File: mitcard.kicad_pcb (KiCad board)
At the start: 2 copper layers, 91 x 55 mm, 13 parts, among them J1 MJ-4PP-9, J2 MJ-4PP-9, SW1 SW_PUSH, SW2 SW_PUSH, SW3 SW_PUSH, SW4 SW_PUSH, U1 Teensy-LC

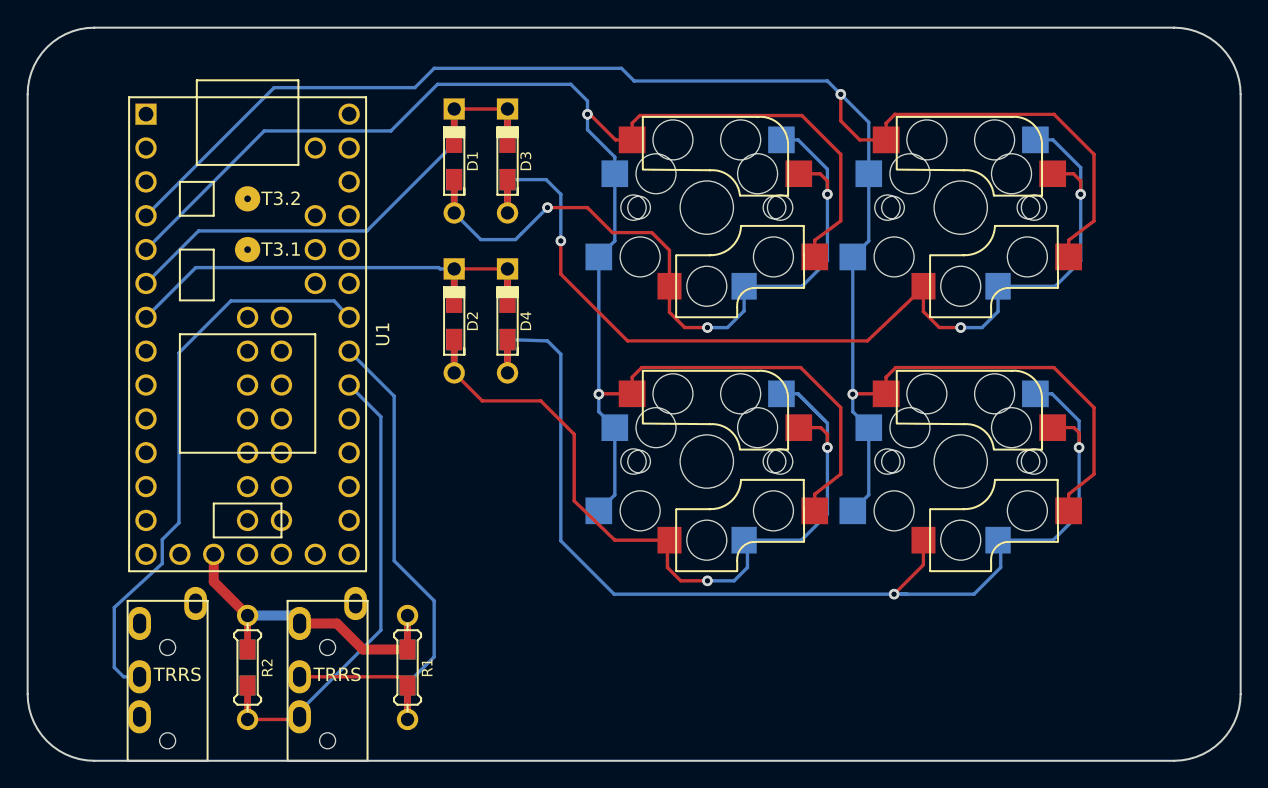
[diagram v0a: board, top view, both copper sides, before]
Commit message: タッチセンサー部を除いて仮配線完了？
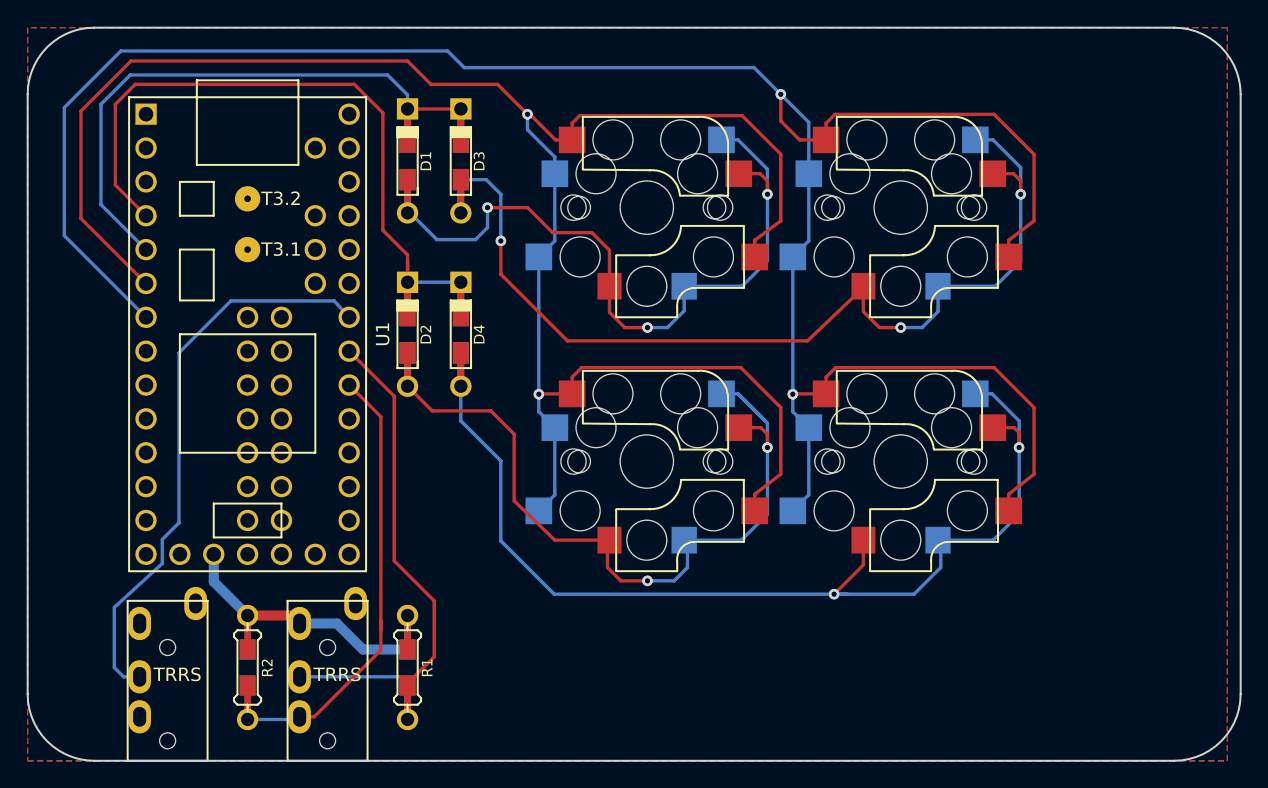
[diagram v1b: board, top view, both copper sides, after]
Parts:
- moved SW1 4.50 mm to (96.5, 63.5)
- moved SW2 4.50 mm to (96.5, 82.5)
- moved SW3 4.50 mm to (115.5, 63.5)
- moved SW4 4.50 mm to (115.5, 82.5)
- moved D2 3.64 mm to (78.5, 73.0)
- moved D4 3.64 mm to (82.5, 73.0)
- moved D1 3.50 mm to (78.5, 60.0)
- moved D3 3.50 mm to (82.5, 60.0)
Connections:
- U1 pad 4: col1 -> row1
- U1 pad 5: col0 -> row0
- U1 pad 6: row0 -> col0
- U1 pad 7: row1 -> col1
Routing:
- net row1: track 30.5 -> 49.0 mm
- net col1: track 153.5 -> 171.2 mm
- net col0: track 132.7 -> 144.6 mm
- net row0: track 33.7 -> 41.9 mm
- net Net-(D4-Pad2): track 83.3 -> 77.7 mm
- net /SDA: track 32.4 -> 34.1 mm
- net Net-(D1-Pad2): track 54.0 -> 55.2 mm
- net /col1row0: track 73.4 -> 72.4 mm
- added copper zone on B.Cu, net GND
- added copper zone on F.Cu, net GND

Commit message: INT ピン変更
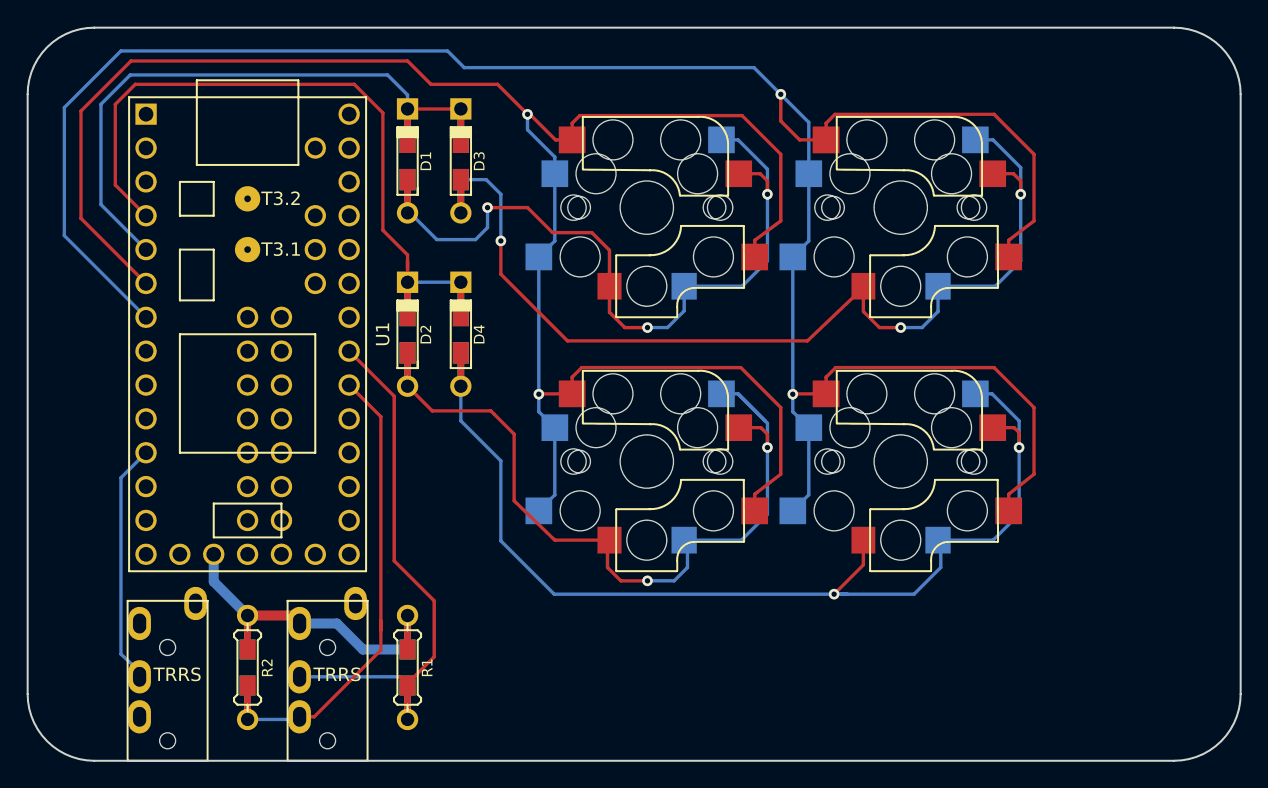
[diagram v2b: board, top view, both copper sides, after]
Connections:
- U1 pad 11: Net-(U1-Pad11) -> /INT
- U1 pad 27: /INT -> Net-(U1-Pad27)
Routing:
- net /INT: track 42.8 -> 18.2 mm
- removed copper zone on B.Cu, net GND
- removed copper zone on F.Cu, net GND

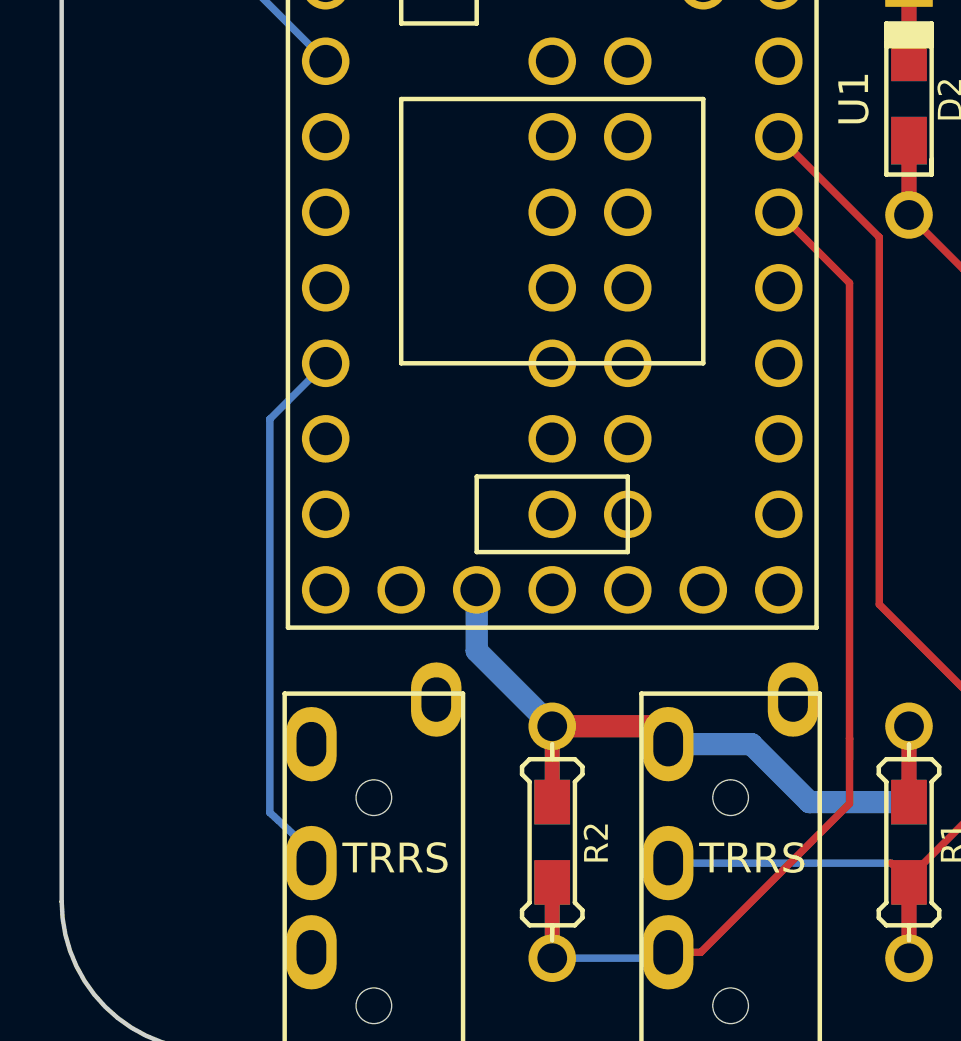
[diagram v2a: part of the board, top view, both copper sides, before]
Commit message: SPI と I2C を引っ張り出しておく
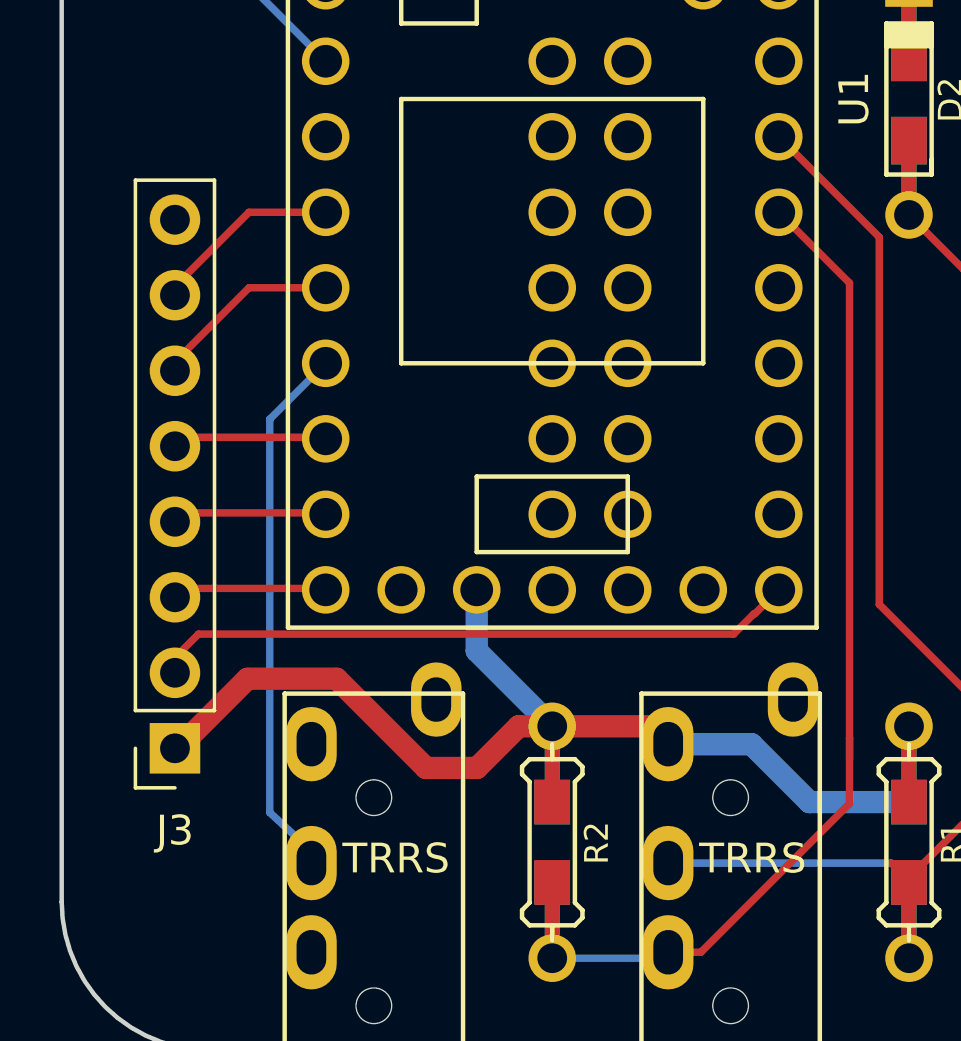
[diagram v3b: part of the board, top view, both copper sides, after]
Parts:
- added J3: Conn_01x08, Connector_PinSocket_2.54mm:PinSocket_1x08_P2.54mm_Vertical, F.Cu at (53.8, 94.8)
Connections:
- U1 pad 10: Net-(U1-Pad10) -> TX
- U1 pad 12: Net-(U1-Pad12) -> CS
- U1 pad 13: Net-(U1-Pad13) -> MOSI
- U1 pad 14: Net-(U1-Pad14) -> MISO
- U1 pad 20: Net-(U1-Pad20) -> SCK
- U1 pad 9: Net-(U1-Pad9) -> RX
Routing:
- net SCK: track 0.00 -> 21.5 mm
- net /3.3V: track 18.7 -> 34.2 mm
- net TX: track 0.00 -> 6.10 mm
- net RX: track 0.00 -> 6.10 mm
- net MISO: track 0.00 -> 5.09 mm
- net CS: track 0.00 -> 5.09 mm
- net MOSI: track 0.00 -> 5.09 mm

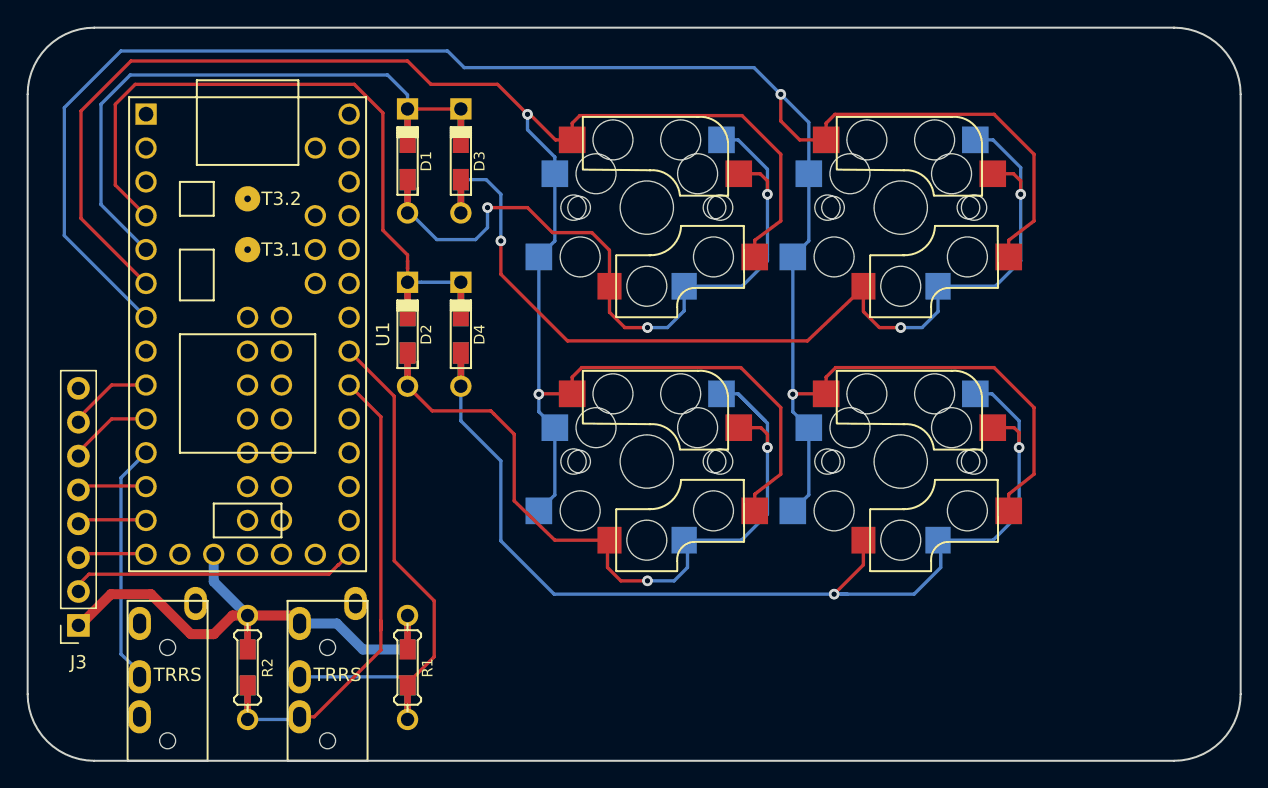
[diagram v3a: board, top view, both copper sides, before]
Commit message: タッチパッド部も書いた
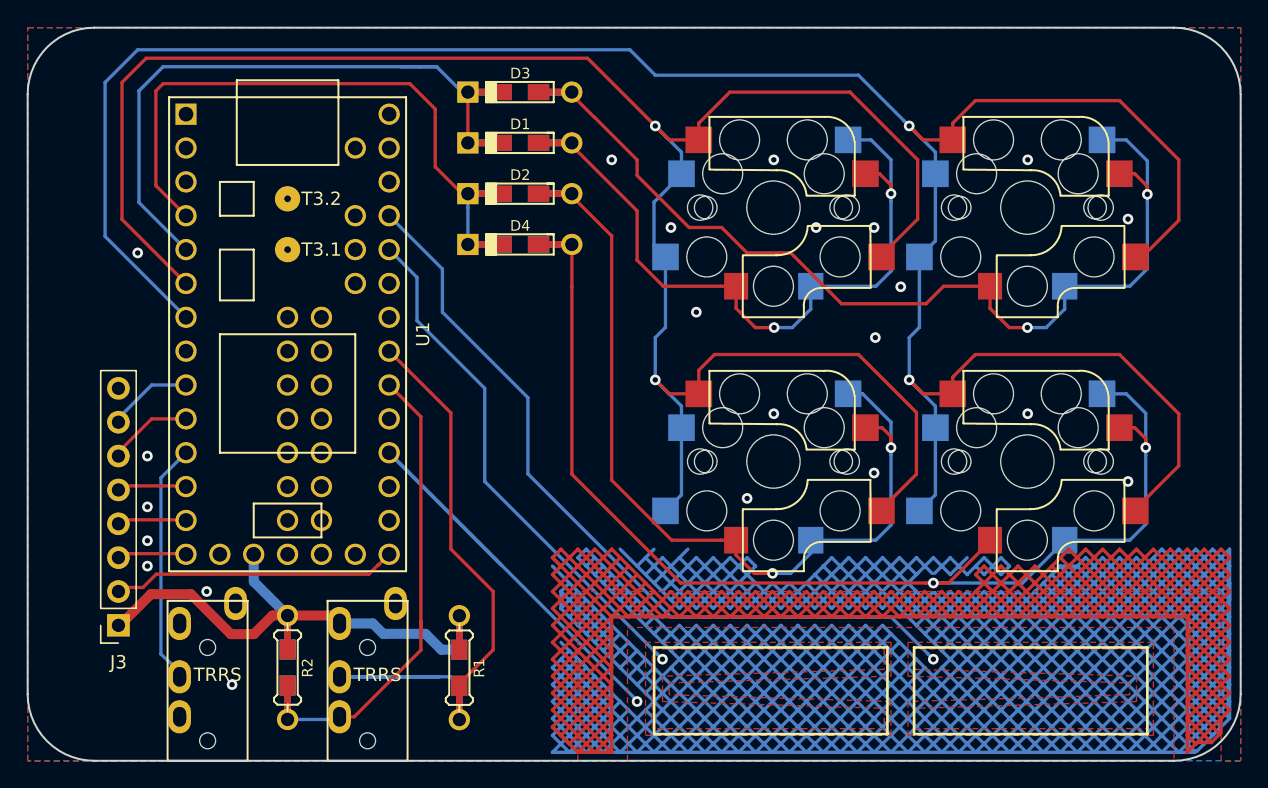
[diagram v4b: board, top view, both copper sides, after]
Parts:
- moved D2 13.5 mm to (86.9, 62.5), turned to 180 degrees
- moved SW1 9.50 mm to (106.0, 63.5)
- moved SW2 9.50 mm to (106.0, 82.5)
- moved SW3 9.50 mm to (125.0, 63.5)
- moved SW4 9.50 mm to (125.0, 82.5)
- moved D1 8.53 mm to (86.9, 58.6), turned to 180 degrees
- moved D4 8.06 mm to (86.9, 66.3), turned to 180 degrees
- moved D3 6.80 mm to (86.9, 54.8), turned to 180 degrees
- moved R1 3.89 mm to (82.4, 98.0)
- moved J1 3.00 mm to (75.5, 105.0)
- moved J2 3.00 mm to (63.5, 105.0)
- moved J3 3.00 mm to (56.8, 94.8)
- moved R2 3.00 mm to (69.5, 98.0)
- moved U1 3.00 mm to (69.5, 73.0)
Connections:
- U1 pad 32: Net-(U1-Pad32) -> GND
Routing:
- net GND: track 0.00 -> 2139.7 mm, vias 0 -> 22
- net Net-(U1-Pad30): track 0.00 -> 59.9 mm, vias 0 -> 1
- net Net-(U1-Pad29): track 0.00 -> 39.2 mm, vias 0 -> 1
- net Net-(U1-Pad23): track 0.00 -> 38.3 mm, vias 0 -> 1
- net col0: track 144.6 -> 158.2 mm
- net col1: track 171.2 -> 182.1 mm
- net /SCL: track 38.1 -> 48.1 mm
- net Net-(D4-Pad2): track 77.7 -> 85.7 mm
- net row0: track 41.9 -> 47.6 mm
- net Net-(D2-Pad2): track 59.4 -> 64.6 mm
- net row1: track 49.0 -> 45.4 mm
- net Net-(D1-Pad2): track 55.2 -> 52.2 mm, vias 3 -> 2
- net /3.3V: track 34.2 -> 35.1 mm
- net /col1row0: track 72.4 -> 73.2 mm, vias 3 -> 2
- added copper zone on B.Cu, net GND
- added copper zone on F.Cu, net GND
- added copper zone on F.Cu, net Net-(U1-Pad23)
- added copper zone on F.Cu, net Net-(U1-Pad29)
- added copper zone on F.Cu, net Net-(U1-Pad30)

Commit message: 記名
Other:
- board text added: "mitcard rev.1 Designed by mitaroThanken"
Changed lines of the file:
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@@
   (general
     (thickness 1.6)
-    (drawings 31)
+    (drawings 32)
     (tracks 932)
     (zones 0)
@@
     )
   )
+  (gr_text "mitcard rev.1\nDesigned by mitaroThanken" (at 115.405 99.285) (layer B.SilkS)
+    (effects (font (size 1.5 1.5) (thickness 0.3)) (justify mirror))
+  )
+  (gr_line (start 134 96.5) (end 116.5 96.5) (layer F.SilkS) (width 0.2))
+  (gr_line (start 134 96.5) (end 134 103) (layer F.SilkS) (width 0.2))
+  (gr_line (start 116.5 103) (end 134 103) (layer F.SilkS) (width 0.2))
+  (gr_line (start 116.5 96.5) (end 116.5 103) (layer F.SilkS) (width 0.2))
+  (gr_line (start 114.5 103) (end 114.5 96.5) (layer F.SilkS) (width 0.2))
+  (gr_line (start 97 103) (end 114.5 103) (layer F.SilkS) (width 0.2))
+  (gr_line (start 97 96.5) (end 97 103) (layer F.SilkS) (width 0.2))
+  (gr_line (start 114.5 96.5) (end 97 96.5) (layer F.SilkS) (width 0.2))
   (dimension 17.5 (width 0.3) (layer Dwgs.User)
     (gr_text "17.500 mm" (at 125.25 109.1) (layer Dwgs.User)
@@
     (arrow2b (pts (xy 97 107) (xy 98.126504 106.413579)))
   )
-  (gr_line (start 97 96.5) (end 97 103) (layer F.SilkS) (width 0.2))
-  (gr_line (start 134 96.5) (end 134 103) (layer F.SilkS) (width 0.2))
-  (gr_line (start 134 96.5) (end 116.5 96.5) (layer F.SilkS) (width 0.2))
-  (gr_line (start 116.5 103) (end 134 103) (layer F.SilkS) (width 0.2))
-  (gr_line (start 116.5 96.5) (end 116.5 103) (layer F.SilkS) (width 0.2))
-  (gr_line (start 114.5 96.5) (end 97 96.5) (layer F.SilkS) (width 0.2))
-  (gr_line (start 114.5 103) (end 114.5 96.5) (layer F.SilkS) (width 0.2))
-  (gr_line (start 97 103) (end 114.5 103) (layer F.SilkS) (width 0.2))
   (dimension 10 (width 0.3) (layer Dwgs.User)
     (gr_text "10.000 mm" (at 152.1 100 270) (layer Dwgs.User)
